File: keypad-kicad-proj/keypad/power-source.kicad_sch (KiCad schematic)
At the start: 12 parts, among them J1 Screw_Terminal_01x02, Q3 IRF9393TRPBF, U2 TLV75901PDRVT

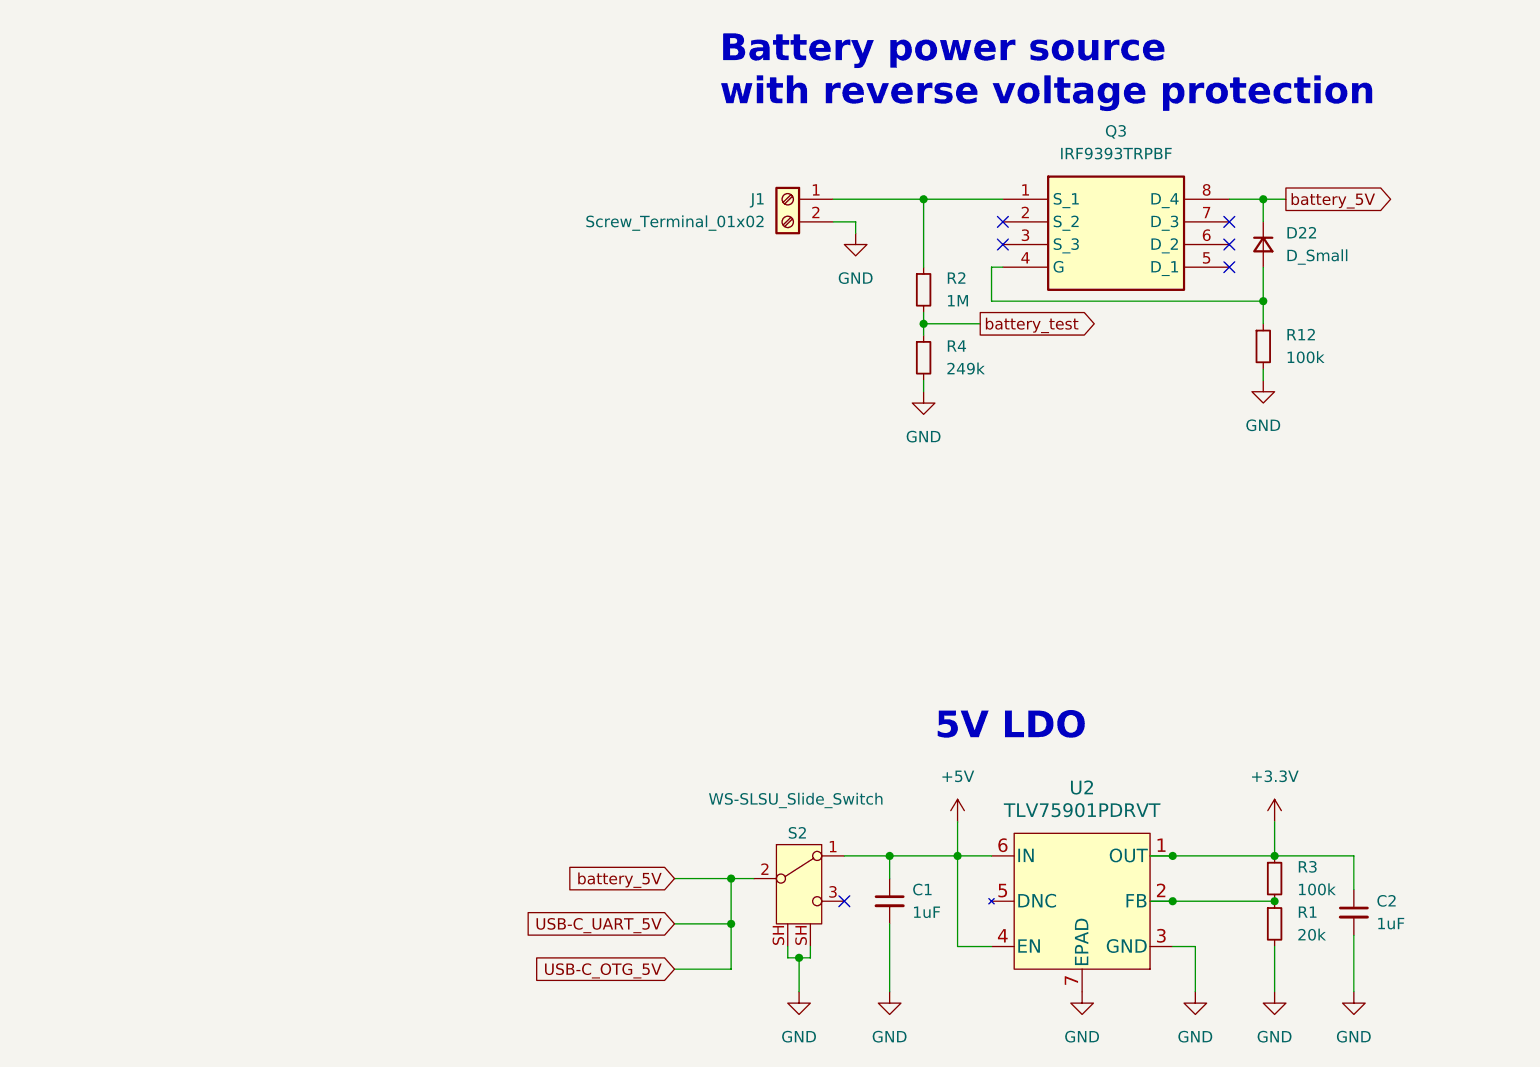
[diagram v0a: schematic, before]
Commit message: add battery charging circuit
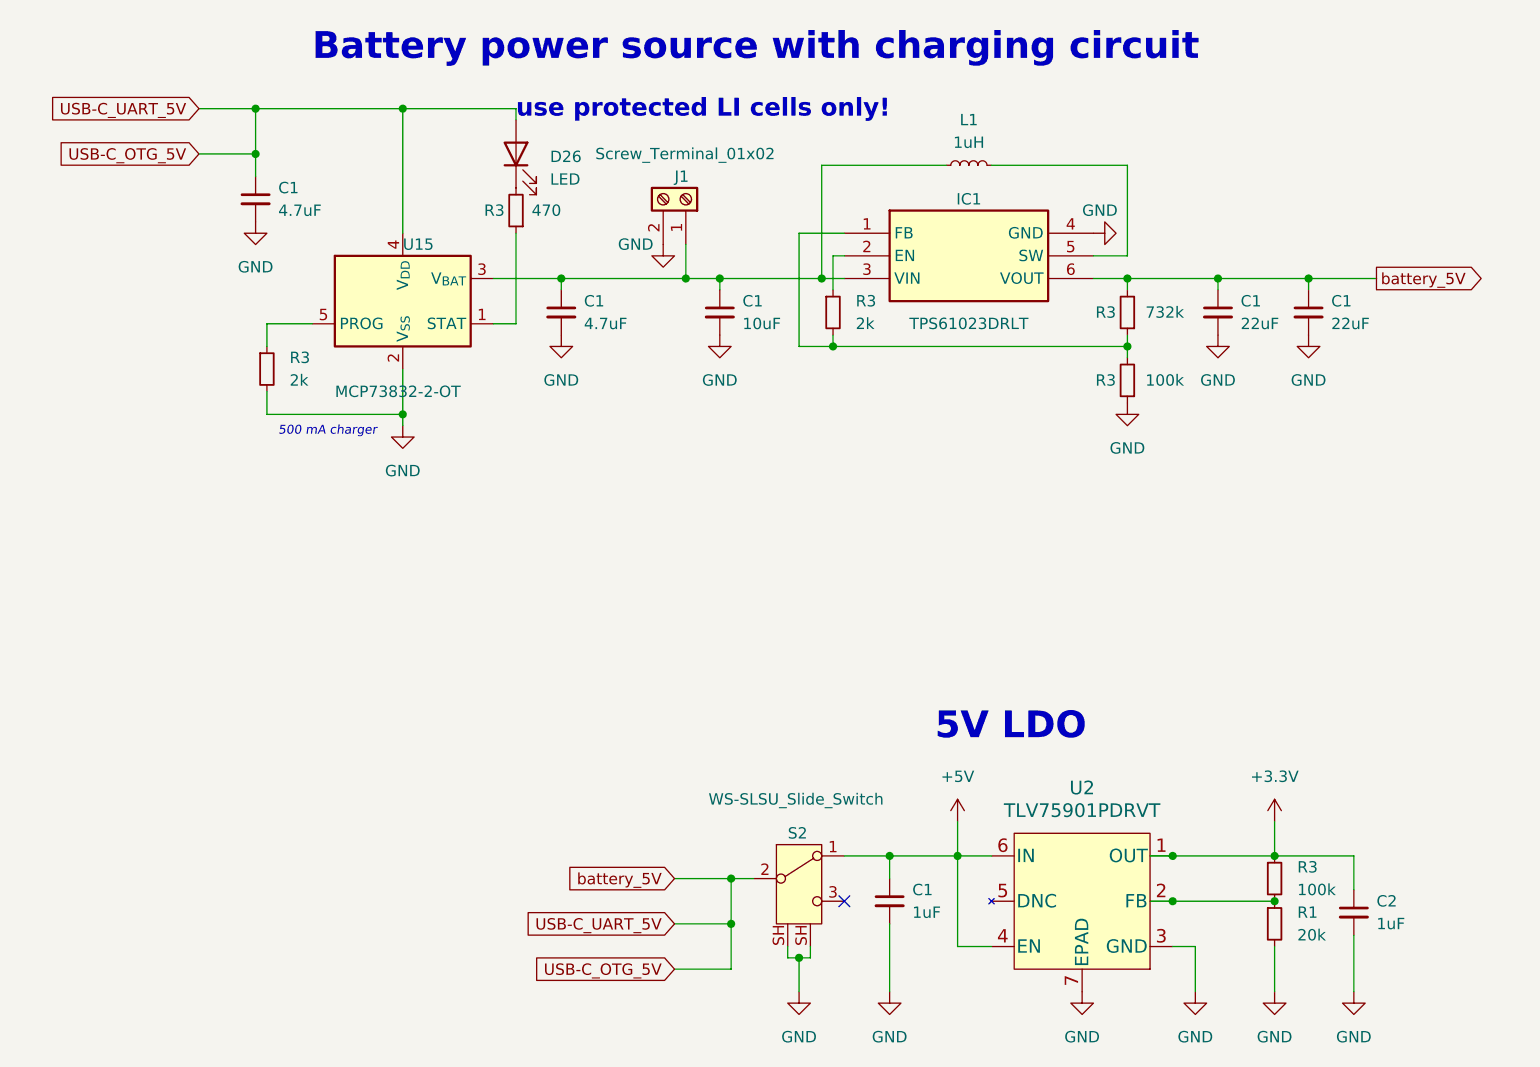
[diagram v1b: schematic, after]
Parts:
- removed D22: D_Small, Diode_SMD:D_SOD-123, symbol Device:D_Small
- removed Q3: IRF9393TRPBF, PUT_RocketLab_other:SOIC127P600X175-8N, symbol PUTRocketLab_semiconductors:IRF9393TRPBF
- removed R12: 100k, Resistor_SMD:R_0805_2012Metric, symbol PutRocketLab_RCL:R_Small
- removed R2: 1M, Resistor_SMD:R_0805_2012Metric, symbol PutRocketLab_RCL:R_Small
- removed R4: 249k, Resistor_SMD:R_0603_1608Metric, symbol PutRocketLab_RCL:R_Small
- added C1 (x2): 22uF, Capacitor_SMD:C_0603_1608Metric, symbol PutRocketLab_RCL:C_Small
- added C1: 10uF, Capacitor_SMD:C_0603_1608Metric, symbol PutRocketLab_RCL:C_Small
- added C1 (x2): 4.7uF, Capacitor_SMD:C_0603_1608Metric, symbol PutRocketLab_RCL:C_Small
- added D26: LED, LED_SMD:LED_0805_2012Metric_Pad1.15x1.40mm_HandSolder, symbol PUTRocketLab_semiconductors:LED
- added IC1: TPS61023DRLT, PUT_RocketLab_IC:TPS61023, symbol PUT_RocketLab_IC:TPS61023DRLT
- added L1: 1uH, Inductor_SMD:L_Bourns_SRP1038C_10.0x10.0mm, symbol PutRocketLab_RCL:L_Small
- added R3: 470, Resistor_SMD:R_0805_2012Metric, symbol PutRocketLab_RCL:R_Small
- added R3 (x2): 2k, Resistor_SMD:R_0805_2012Metric, symbol PutRocketLab_RCL:R_Small
- added R3: 100k, Resistor_SMD:R_0805_2012Metric, symbol PutRocketLab_RCL:R_Small
- added R3: 732k, Resistor_SMD:R_0805_2012Metric, symbol PutRocketLab_RCL:R_Small
- added U15: MCP73832-2-OT, Package_TO_SOT_SMD:SOT-23-5, symbol Battery_Management:MCP73832-2-OT
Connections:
- net GND: now also C1.2, C1.2, C1.2, C1.2, C1.2, IC1.4 (GND), R3.1, R3.2, U15.2 (V_{SS})
- net USB-C_OTG_5V: now also C1.1, C1.1, C1.1, D26.2 (A), IC1.6 (VOUT), R3.2, U15.4 (V_{DD})
- net at J1.1 (Pin_1): now also C1.1, C1.1, IC1.3 (VIN), L1.1, U15.3 (V_{BAT})
- new net: R3.1, U15.1 (STAT)
- new net: D26.1 (K), R3.2
- new net: R3.1, U15.5 (PROG)
- new net: IC1.5 (SW), L1.2
- new net: IC1.1 (FB), R3.1, R3.2, R3.2
- new net: IC1.2 (EN), R3.1
- no-connect marks 6 -> 1
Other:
- note added: "500 mA charger"
- note added: "Battery power source with charging circuit"
- note added: "use protected LI cells only!"
- note removed: "Battery power source with reverse voltage protection"
- moved on the sheet: J1

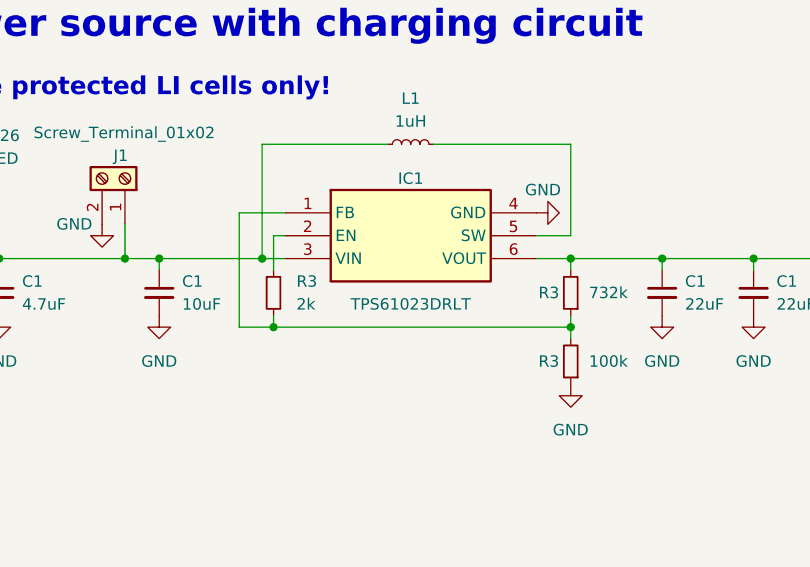
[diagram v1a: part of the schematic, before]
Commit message: finish charging circuit, add description in front silk screen, prepare for production
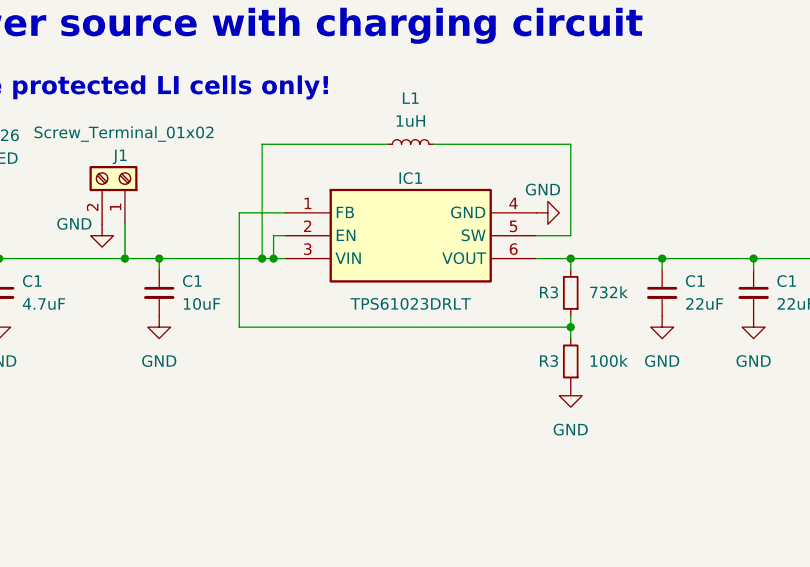
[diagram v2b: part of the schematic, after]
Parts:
- removed R3: 2k, Resistor_SMD:R_0805_2012Metric, symbol PutRocketLab_RCL:R_Small
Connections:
- net at C1.1, C1.1, IC1.3 (VIN)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: now also IC1.2 (EN)
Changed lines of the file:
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@@
   (junction (at 177.8 55.88) (diameter 0) (color 0 0 0 0)
   )
+  (junction (at 124.46 55.88) (diameter 0) (color 0 0 0 0)
+  )
   (junction (at 138.43 120.65) (diameter 0) (color 0 0 0 0)
   )
@@
   )
   (junction (at 157.48 55.88) (diameter 0) (color 0 0 0 0)
-  )
-  (junction (at 124.46 63.5) (diameter 0) (color 0 0 0 0)
   )
   (junction (at 173.99 120.65) (diameter 0) (color 0 0 0 0)
@@
     (stroke (width 0) (type default))
   )
-  (wire (pts (xy 124.46 63.5) (xy 157.48 63.5))
+  (wire (pts (xy 120.65 63.5) (xy 157.48 63.5))
     (stroke (width 0) (type default))
   )
@@
     (stroke (width 0) (type default))
   )
-  (wire (pts (xy 120.65 63.5) (xy 124.46 63.5))
-    (stroke (width 0) (type default))
-  )
   (wire (pts (xy 107.95 52.07) (xy 107.95 55.88))
     (stroke (width 0) (type default))
@@
     (stroke (width 0) (type default))
   )
-  (wire (pts (xy 124.46 62.23) (xy 124.46 63.5))
-    (stroke (width 0) (type default))
-  )
   (wire (pts (xy 182.88 120.65) (xy 173.99 120.65))
     (stroke (width 0) (type default))
@@
     (stroke (width 0) (type default))
   )
+  (wire (pts (xy 124.46 55.88) (xy 125.73 55.88))
+    (stroke (width 0) (type default))
+  )
   (wire (pts (xy 177.8 55.88) (xy 185.42 55.88))
     (stroke (width 0) (type default))
@@
     (stroke (width 0) (type default))
   )
-  (wire (pts (xy 124.46 57.15) (xy 124.46 53.34))
-    (stroke (width 0) (type default))
-  )
   (wire (pts (xy 120.65 132.08) (xy 120.65 135.89))
     (stroke (width 0) (type default))
@@
     (stroke (width 0) (type default))
   )
-  (wire (pts (xy 123.19 55.88) (xy 125.73 55.88))
+  (wire (pts (xy 123.19 55.88) (xy 124.46 55.88))
     (stroke (width 0) (type default))
   )
@@
   )
   (wire (pts (xy 76.2 36.83) (xy 88.9 36.83))
+    (stroke (width 0) (type default))
+  )
+  (wire (pts (xy 124.46 53.34) (xy 124.46 55.88))
     (stroke (width 0) (type default))
   )
@@
         )
       )
-    )
-  )
-  (symbol (lib_id "PutRocketLab_RCL:R_Small") (at 124.46 59.69 0) (unit 1)
-    (in_bom yes) (on_board yes) (dnp no)
-    (property "Reference" "R3" (at 127 58.42 0)
-      (effects (font (size 1.27 1.27)) (justify left))
-    )
-    (property "Value" "2k" (at 127 60.96 0)
-      (effects (font (size 1.27 1.27)) (justify left))
-    )
-    (property "Footprint" "Resistor_SMD:R_0805_2012Metric" (at 124.46 59.69 0)
-      (effects (font (size 1.27 1.27)) hide)
-    )
-    (property "Datasheet" "~" (at 124.46 59.69 0)
-      (effects (font (size 1.27 1.27)) hide)
-    )
-    (pin "1")
-    (pin "2")
-    (instances
-      (project "keypad"
-        (path "/26078c39-1d91-4154-8719-da74cb453e74"
-          (reference "R3") (unit 1)
-        )
-        (path "/26078c39-1d91-4154-8719-da74cb453e74/3e174945-0f14-4777-84ae-d28e4ef4eec5"
-          (reference "R24") (unit 1)
-        )
-      )

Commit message: update datasheets
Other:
- note added: "use protected Li cells only!"
- note removed: "use protected LI cells only!"
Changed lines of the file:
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@@
     (stroke (width 0) (type default))
   )
-  (text "use protected LI cells only!" (at 88.9 38.1 0)
+  (text "use protected Li cells only!" (at 88.9 38.1 0)
     (effects (font (size 2 2) (thickness 0.4) bold (color 255 71 100 1)) (justify left bottom))
   )
